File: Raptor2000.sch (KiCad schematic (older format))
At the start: 5 parts, among them SW1 SW_Push, U4 ESP-12E

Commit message: updates
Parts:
- removed R4: R_Small, Resistor_SMD:R_0603_1608Metric, symbol Device:R_Small
- removed SW1: SW_Push, Button_Switch_SMD:SW_SPST_EVPBF, symbol Switch:SW_Push
- removed U4: ESP-12E, RF_Module:ESP-12E, symbol RF_Module:ESP-12E
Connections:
- net labels added: +3.3V
- net labels removed: +BATT
- wire segments 57 -> 50
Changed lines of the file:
@@
 EESchema Schematic File Version 4
+LIBS:Raptor2000-cache
 EELAYER 29 0
 EELAYER END
@@
 JTAG_TMS
 Wire Wire Line
-	1800 1400 1900 1400
-Wire Wire Line
 	1900 1400 1900 1300
-Wire Wire Line
-	1800 1500 1900 1500
-Wire Wire Line
-	1900 1500 1900 1600
-$Comp
-L power:GND #PWR0149
-U 1 1 5C8F5DB2
-P 1900 1600
-F 0 "#PWR0149" H 1900 1350 50  0001 C CNN
-F 1 "GND" H 1905 1427 50  0000 C CNN
-F 2 "" H 1900 1600 50  0001 C CNN
-F 3 "" H 1900 1600 50  0001 C CNN
-	1    1900 1600
-	1    0    0    -1
-$EndComp
-$Comp
-L power:+BATT #PWR0150
-U 1 1 5C8F5ED8
-P 1900 1300
-F 0 "#PWR0150" H 1900 1150 50  0001 C CNN
-F 1 "+BATT" H 1915 1473 50  0000 C CNN
-F 2 "" H 1900 1300 50  0001 C CNN
-F 3 "" H 1900 1300 50  0001 C CNN
-	1    1900 1300
-	1    0    0    -1
-$EndComp
 Wire Wire Line
 	4700 2100 5450 2100
@@
 Wire Wire Line
 	1900 1400 2100 1400
-Connection ~ 1900 1400
 $Comp
 L Device:R_Small R30
@@
 	5450 4750 4700 4750
 $Comp
-L Switch:SW_Push SW1
-U 1 1 5CC76729
-P 1200 1400
-F 0 "SW1" H 1200 1685 50  0000 C CNN
-F 1 "SW_Push" H 1200 1594 50  0000 C CNN
-F 2 "Button_Switch_SMD:SW_SPST_EVPBF" H 1200 1600 50  0001 C CNN
-F 3 "" H 1200 1600 50  0001 C CNN
-	1    1200 1400
+L power:+3.3V #PWR0118
+U 1 1 5CE8B203
+P 1900 1300
+F 0 "#PWR0118" H 1900 1150 50  0001 C CNN
+F 1 "+3.3V" H 1915 1473 50  0000 C CNN
+F 2 "" H 1900 1300 50  0001 C CNN
+F 3 "" H 1900 1300 50  0001 C CNN
+	1    1900 1300
 	1    0    0    -1
 $EndComp
-$Comp
-L Device:R_Small R4
-U 1 1 5CC77AFB
-P 1500 1600
-F 0 "R4" H 1441 1554 50  0000 R CNN
-F 1 "R_Small" H 1441 1645 50  0000 R CNN
-F 2 "Resistor_SMD:R_0603_1608Metric" H 1500 1600 50  0001 C CNN
-F 3 "~" H 1500 1600 50  0001 C CNN
-	1    1500 1600
-	-1   0    0    1
-$EndComp
-$Comp
-L power:GND #PWR0116
-U 1 1 5CC77B03
-P 1500 1800
-F 0 "#PWR0116" H 1500 1550 50  0001 C CNN
-F 1 "GND" H 1505 1627 50  0000 C CNN
-F 2 "" H 1500 1800 50  0001 C CNN
-F 3 "" H 1500 1800 50  0001 C CNN
-	1    1500 1800
-	1    0    0    -1
-$EndComp
-Wire Wire Line
-	1500 1700 1500 1800
-Wire Wire Line
-	1400 1400 1500 1400
-Wire Wire Line
-	1500 1400 1500 1500
-Wire Wire Line
-	1000 1400 900  1400
-$Comp
-L RF_Module:ESP-12E U4
-U 1 1 5CBC1C3D
-P 4500 6400
-F 0 "U4" H 4500 7378 50  0000 C CNN
-F 1 "ESP-12E" H 4500 7287 50  0000 C CNN
-F 2 "RF_Module:ESP-12E" H 4500 6400 50  0001 C CNN
-F 3 "http://wiki.ai-thinker.com/_media/esp8266/esp8266_series_modules_user_manual_v1.1.pdf" H 4150 6500 50  0001 C CNN
-	1    4500 6400
-	1    0    0    -1
-$EndComp

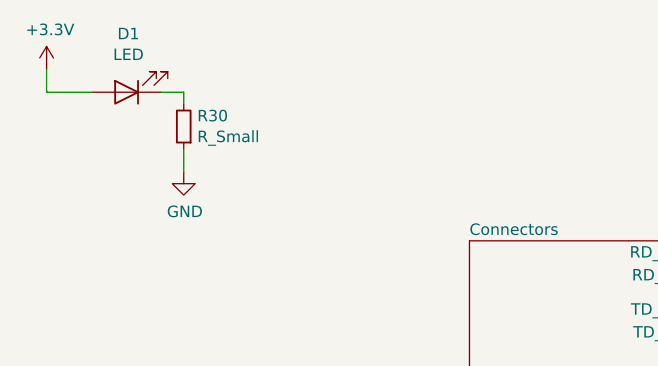
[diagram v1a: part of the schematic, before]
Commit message: fixing some unnamed nets.
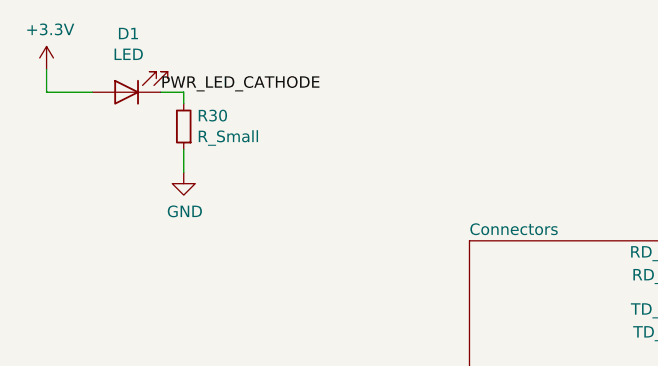
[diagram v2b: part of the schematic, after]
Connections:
- net PWR_LED_CATHODE: now reaches D1.1 (K), R30.2
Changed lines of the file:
@@
 	1    0    0    -1
 $EndComp
+Text Label 2400 1400 0    50   ~ 0
+PWR_LED_CATHODE
 $EndSCHEMATC

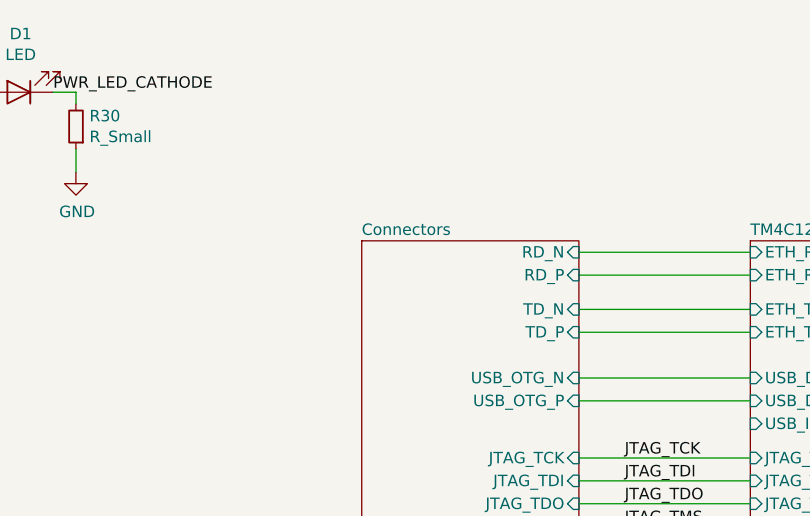
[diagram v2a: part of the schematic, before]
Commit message: Connected the board sense pin to 3.3V to work with the backplane.
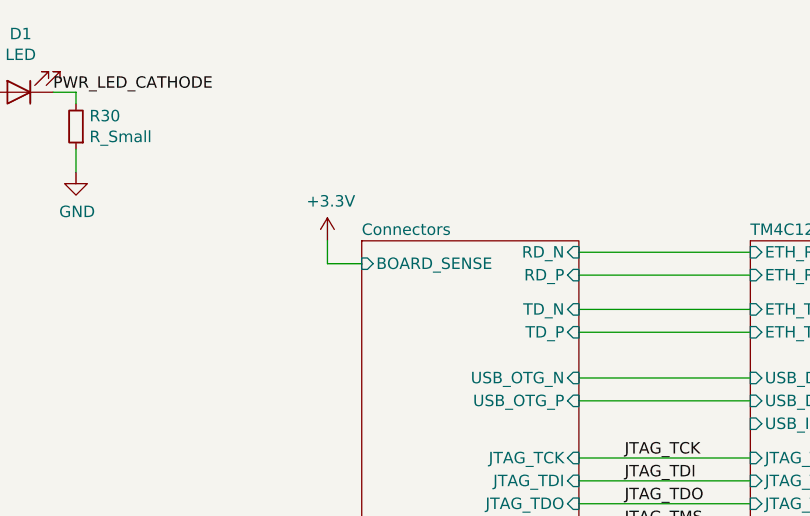
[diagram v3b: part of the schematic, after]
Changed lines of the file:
@@
 EESchema Schematic File Version 4
-LIBS:Raptor2000-cache
 EELAYER 29 0
 EELAYER END
@@
 F22 "ETH_LED0" I R 4700 4650 50
 F23 "ETH_LED1" I R 4700 4750 50
+F24 "BOARD_SENSE" I L 3750 2150 50
 $EndSheet
 Text Label 4900 3000 0    50   ~ 0
@@
 Text Label 2400 1400 0    50   ~ 0
 PWR_LED_CATHODE
+Wire Wire Line
+	3750 2150 3600 2150
+Wire Wire Line
+	3600 2150 3600 2050
+$Comp
+L power:+3.3V #PWR?
+U 1 1 5CF42D9F
+P 3600 2050
+F 0 "#PWR?" H 3600 1900 50  0001 C CNN
+F 1 "+3.3V" H 3615 2223 50  0000 C CNN
+F 2 "" H 3600 2050 50  0001 C CNN
+F 3 "" H 3600 2050 50  0001 C CNN
+	1    3600 2050
+	1    0    0    -1
+$EndComp
 $EndSCHEMATC

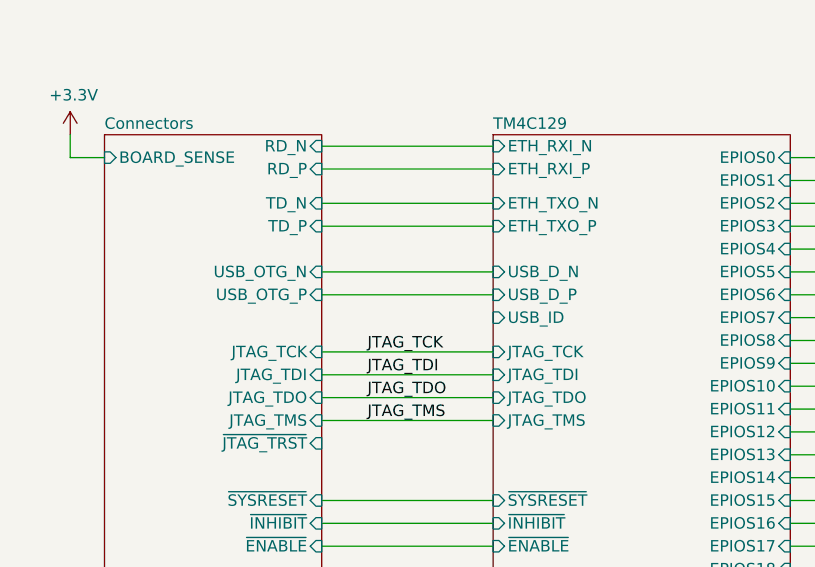
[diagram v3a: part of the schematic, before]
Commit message: Added usb id and usb vbus pins to tm4c circuit. Unconnected on main backplane connector.
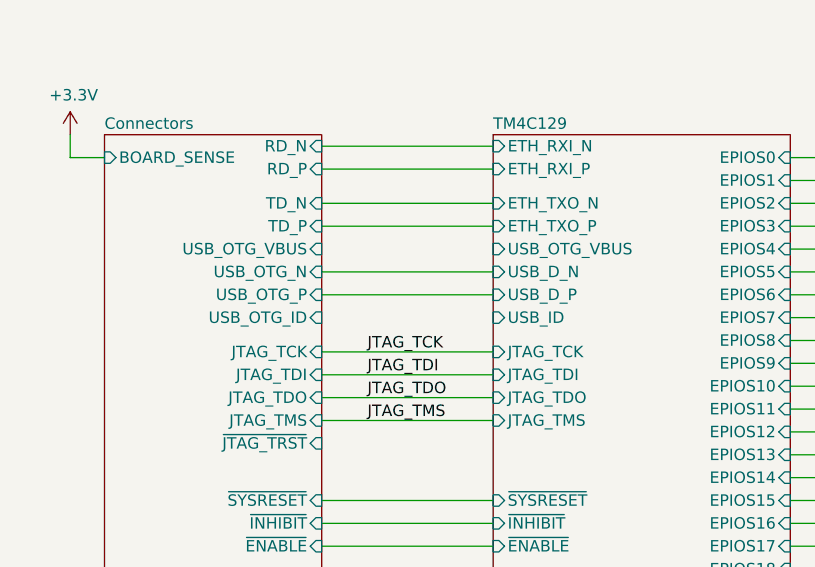
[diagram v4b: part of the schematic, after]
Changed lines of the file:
@@
 F46 "ETH_LED0" I L 5450 4650 50
 F47 "ETH_LED1" I L 5450 4750 50
+F48 "USB_OTG_VBUS" I L 5450 2550 50
 $EndSheet
 $Sheet
@@
 F23 "ETH_LED1" I R 4700 4750 50
 F24 "BOARD_SENSE" I L 3750 2150 50
+F25 "USB_OTG_ID" I R 4700 2850 50
+F26 "USB_OTG_VBUS" I R 4700 2550 50
 $EndSheet
 Text Label 4900 3000 0    50   ~ 0

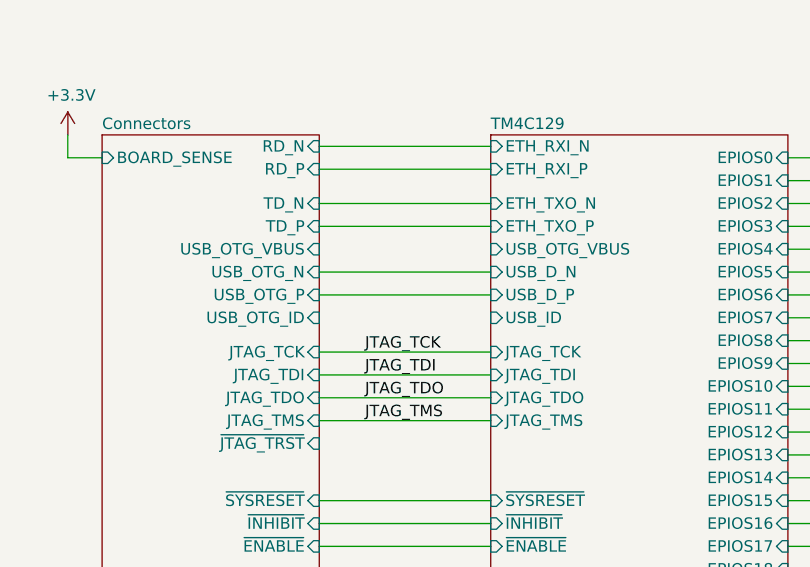
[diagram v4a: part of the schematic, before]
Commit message: initial implementation of vbatt for RTC.
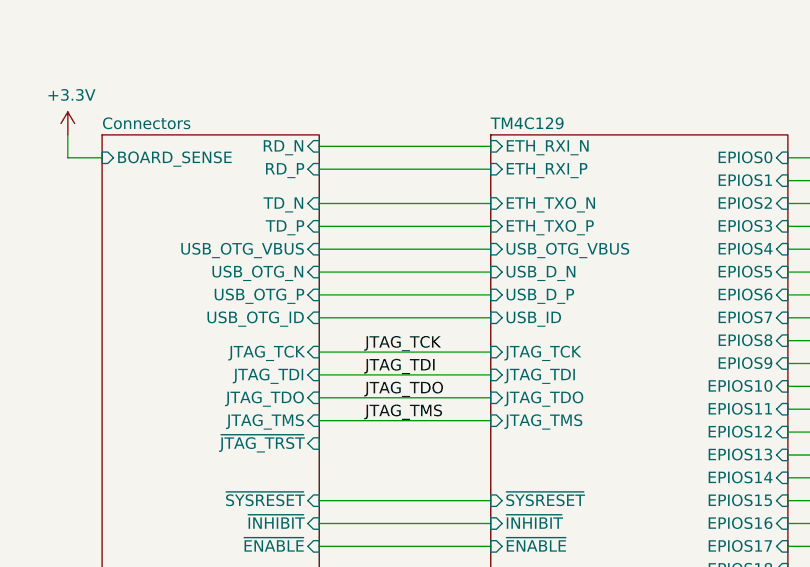
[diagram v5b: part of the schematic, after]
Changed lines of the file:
@@
 EESchema Schematic File Version 4
+LIBS:Raptor2000-cache
 EELAYER 29 0
 EELAYER END
@@
 	3600 2150 3600 2050
 $Comp
-L power:+3.3V #PWR?
+L power:+3.3V #PWR0116
 U 1 1 5CF42D9F
 P 3600 2050
-F 0 "#PWR?" H 3600 1900 50  0001 C CNN
+F 0 "#PWR0116" H 3600 1900 50  0001 C CNN
 F 1 "+3.3V" H 3615 2223 50  0000 C CNN
 F 2 "" H 3600 2050 50  0001 C CNN
@@
 	1    0    0    -1
 $EndComp
+Wire Wire Line
+	4700 2850 5450 2850
+Wire Wire Line
+	4700 2550 5450 2550
 $EndSCHEMATC

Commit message: added nand flash, removed sd card. finished rtc circuit. added leds
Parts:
- removed D1: LED, LED_SMD:LED_0603_1608Metric, symbol Device:LED
- removed R30: R_Small, Resistor_SMD:R_0603_1608Metric, symbol Device:R_Small
- added H1, H2, H3, H4: MountingHole, MountingHole:MountingHole_3.2mm_M3, symbol Mechanical:MountingHole
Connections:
- net labels removed: +3.3V, GND, JTAG_TCK, JTAG_TDI, JTAG_TDO, JTAG_TMS, PWR_LED_CATHODE
- wire segments 54 -> 21

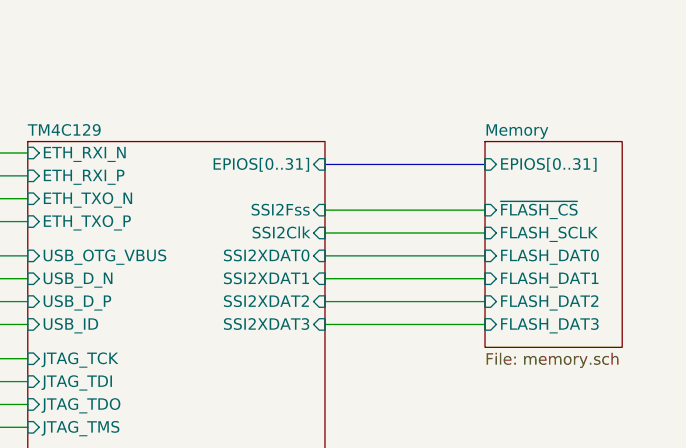
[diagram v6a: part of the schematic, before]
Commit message: fixed misnamed EPI nets.
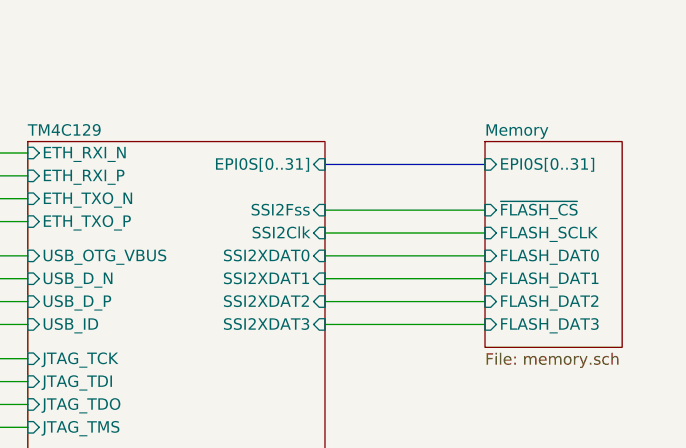
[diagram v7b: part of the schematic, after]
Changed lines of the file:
@@
 F6 "FLASH_DAT3" I L 7450 2850 50
 F7 "~FLASH_CS" I L 7450 2350 50
-F8 "EPIOS[0..31]" I L 7450 2150 50
+F8 "EPI0S[0..31]" I L 7450 2150 50
 $EndSheet
 $Comp
@@
 F21 "SSI2XDAT3" I R 6750 2850 50
 F22 "SSI2XDAT2" I R 6750 2750 50
-F23 "EPIOS[0..31]" I R 6750 2150 50
+F23 "EPI0S[0..31]" I R 6750 2150 50
 $EndSheet
 $EndSCHEMATC

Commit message: updated come component values.
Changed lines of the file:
@@
 F9 "~INHIBIT" I R 4700 3700 50
 F10 "~SYSRESET" I R 4700 3600 50
-F11 "~JTAG_TRST" I R 4700 3400 50
-F12 "JTAG_TMS" I R 4700 3300 50
-F13 "JTAG_TCK" I R 4700 3000 50
-F14 "JTAG_TDI" I R 4700 3100 50
-F15 "JTAG_TDO" I R 4700 3200 50
-F16 "USB_OTG_ID" I R 4700 2850 50
-F17 "USB_OTG_VBUS" I R 4700 2550 50
+F11 "JTAG_TMS" I R 4700 3300 50
+F12 "JTAG_TCK" I R 4700 3000 50
+F13 "JTAG_TDI" I R 4700 3100 50
+F14 "JTAG_TDO" I R 4700 3200 50
+F15 "USB_OTG_ID" I R 4700 2850 50
+F16 "USB_OTG_VBUS" I R 4700 2550 50
 $EndSheet
 Wire Bus Line
